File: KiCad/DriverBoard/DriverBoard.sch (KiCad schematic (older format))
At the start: 5 parts, among them J1 Conn_01x11, J2 Conn_01x05, J4 Conn_01x12, U1 Pico

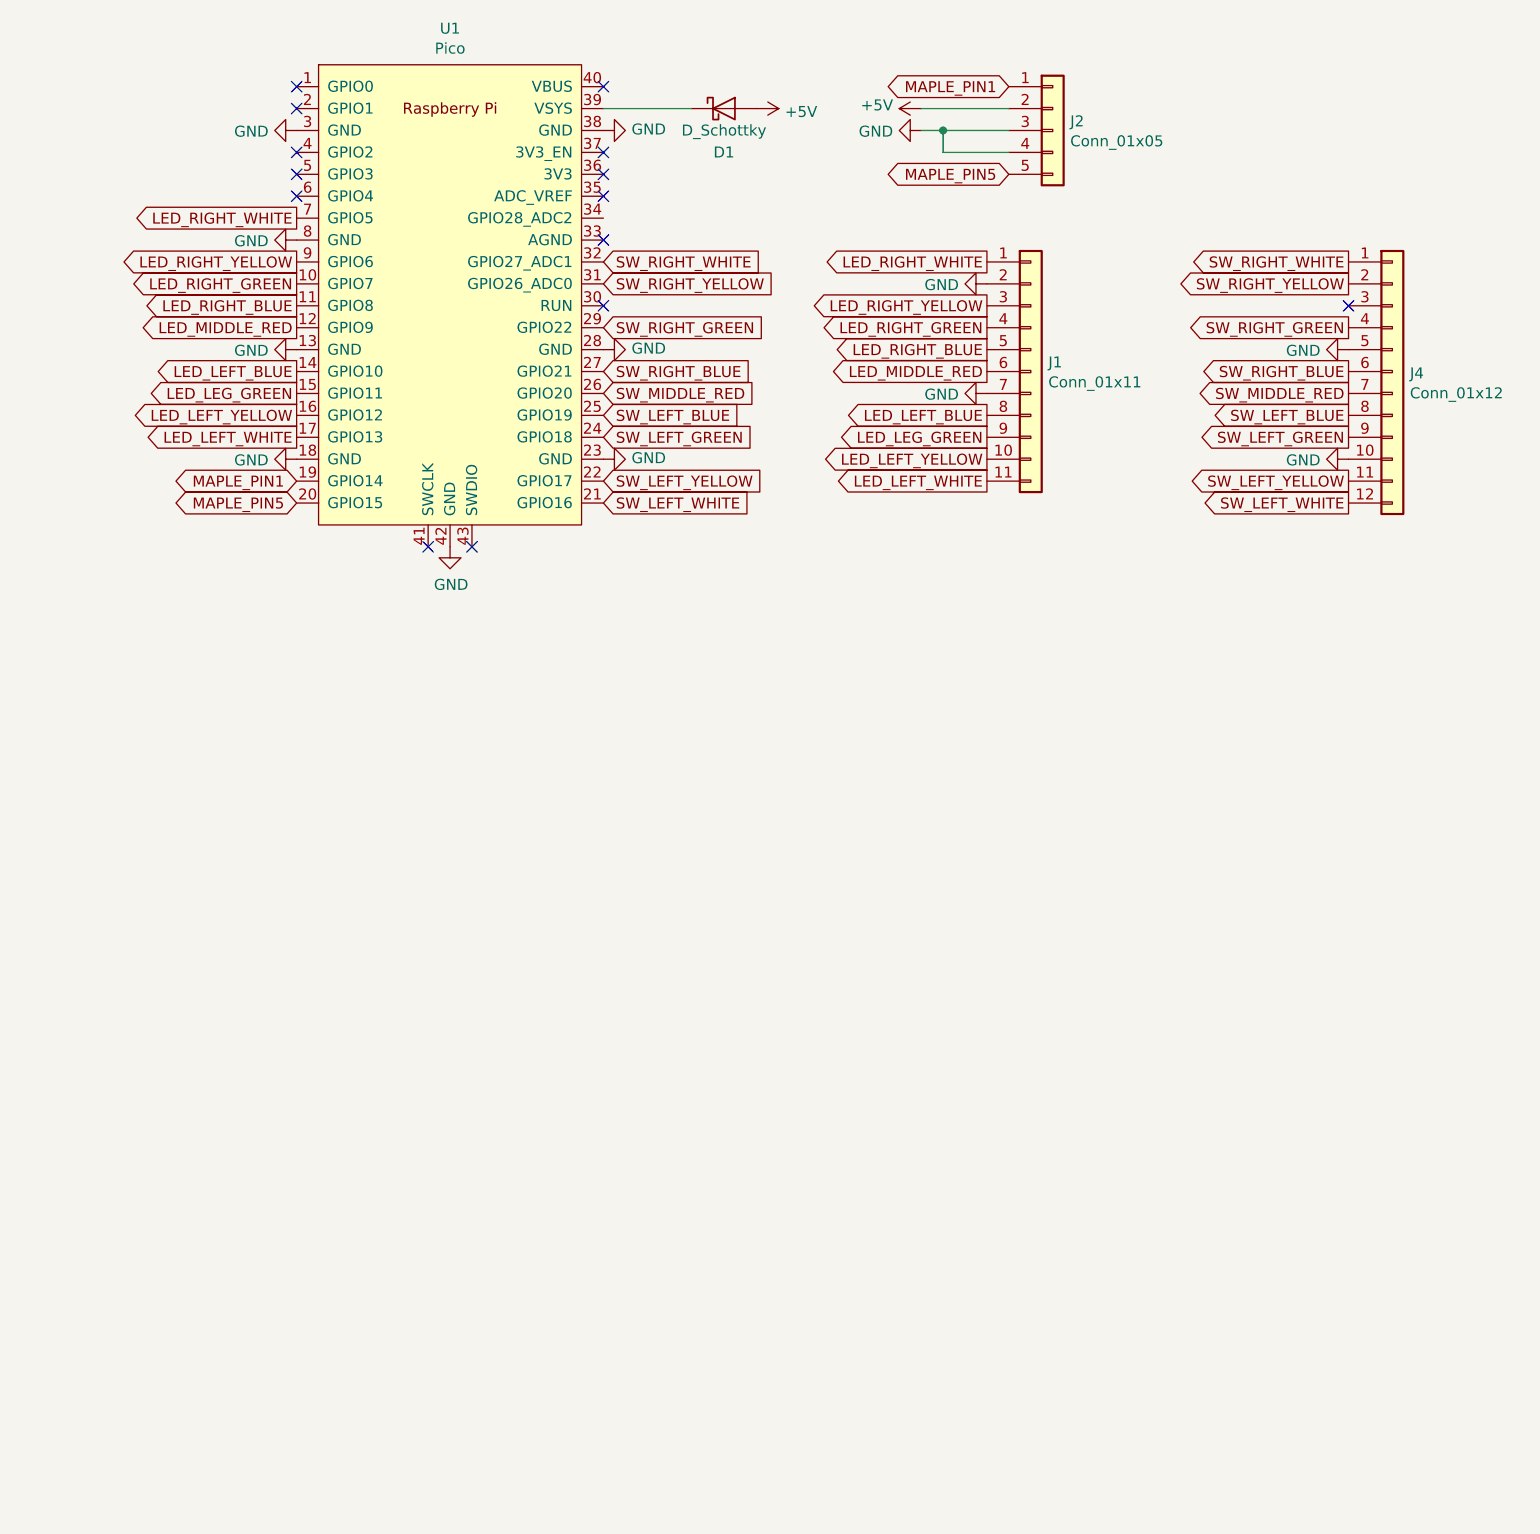
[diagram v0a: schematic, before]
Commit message: Added 5V LED drivers
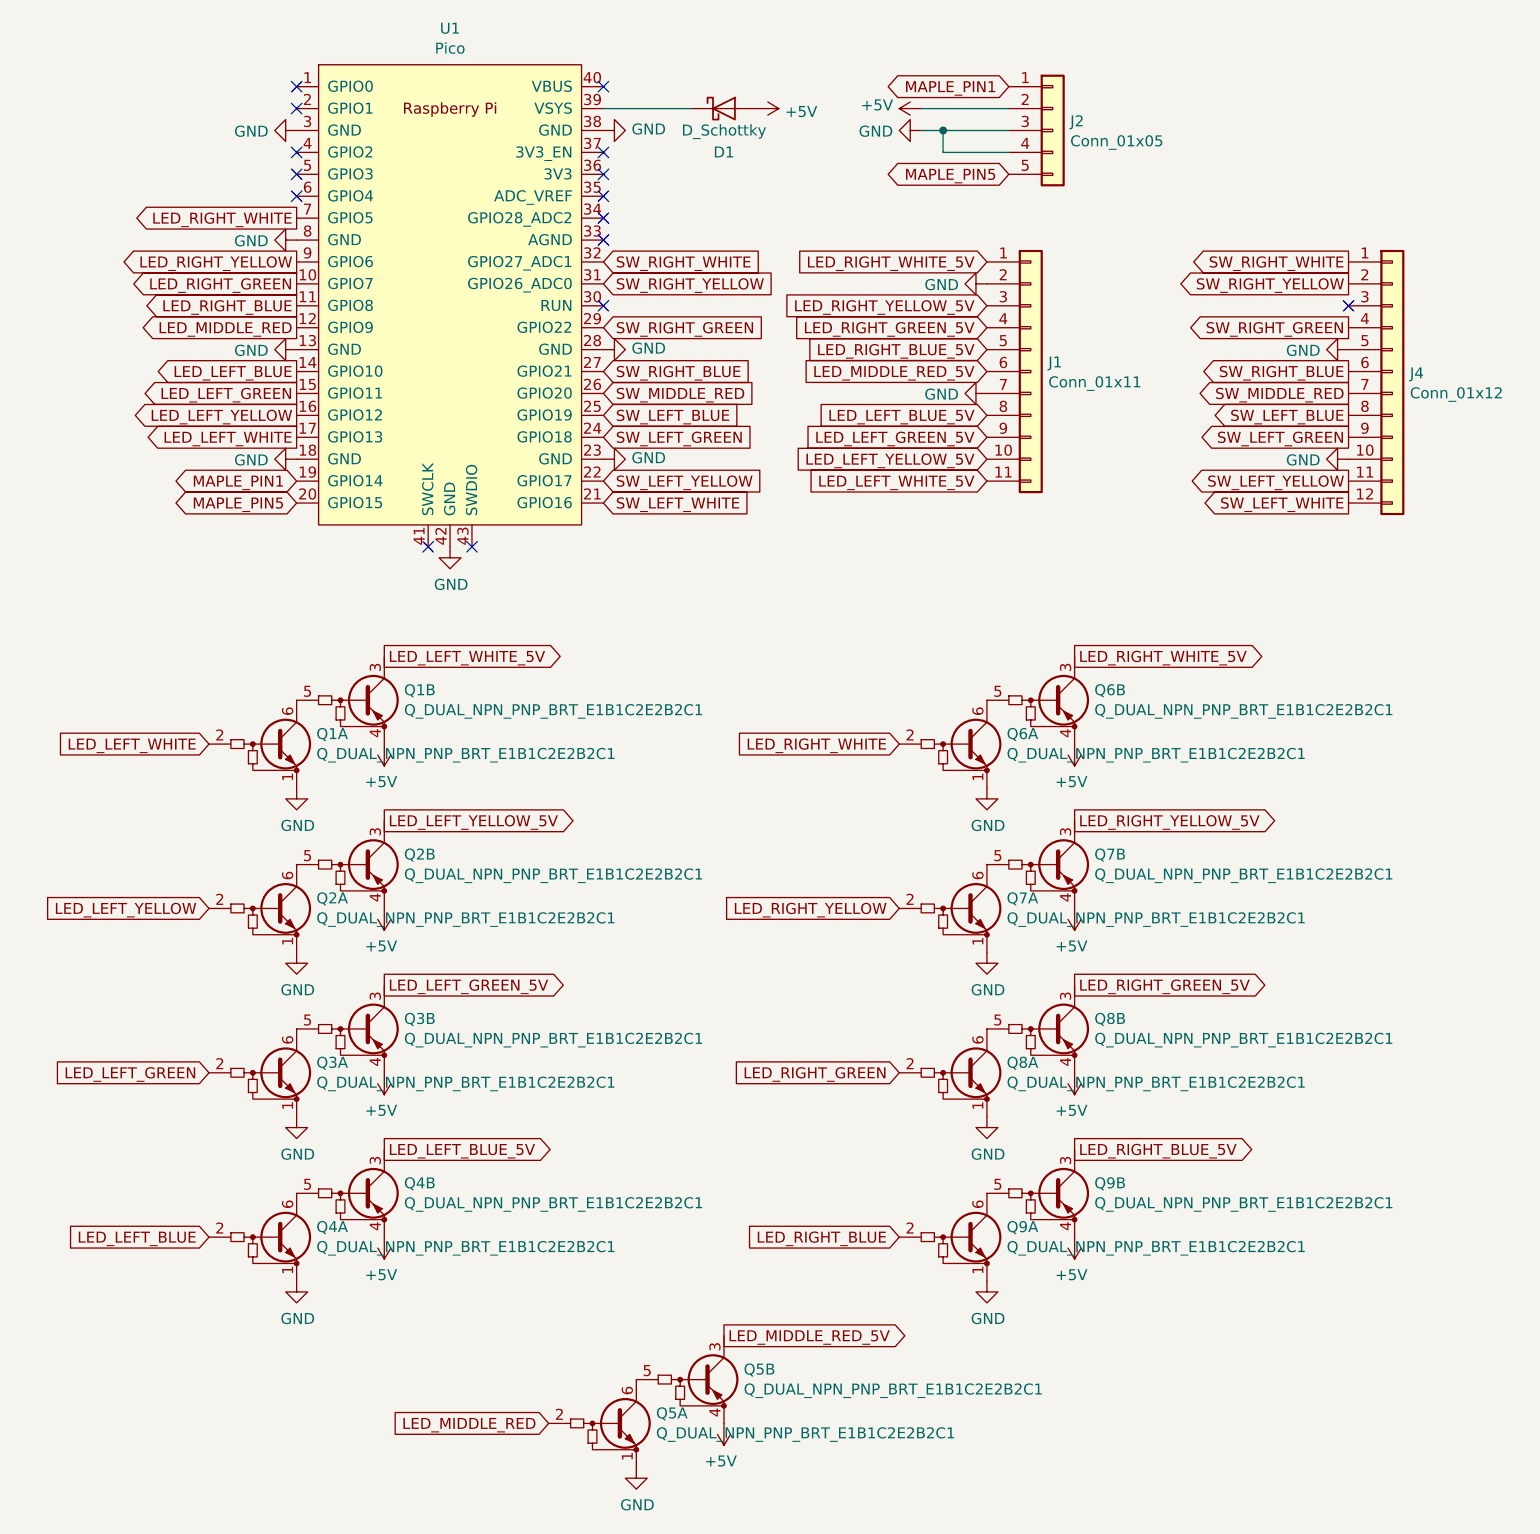
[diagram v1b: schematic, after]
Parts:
- added Q1, Q2, Q3, Q4, Q5, Q6, Q7, Q8, Q9: Q_DUAL_NPN_PNP_BRT_E1B1C2E2B2C1, Package_TO_SOT_SMD:SOT-363_SC-70-6_Handsoldering, symbol Device:Q_DUAL_NPN_PNP_BRT_E1B1C2E2B2C1
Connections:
- net +5V: now also Q1.4 (E1), Q2.4 (E1), Q3.4 (E1), Q4.4 (E1), Q5.4 (E1), Q6.4 (E1), Q7.4 (E1), Q8.4 (E1), Q9.4 (E1)
- net GND: now also Q1.1 (E1), Q2.1 (E1), Q3.1 (E1), Q4.1 (E1), Q5.1 (E1), Q6.1 (E1), Q7.1 (E1), Q8.1 (E1), Q9.1 (E1)
- net LED_LEFT_BLUE: now also Q4.2 (B1); no longer J1.8 (Pin_8)
- net LED_LEFT_WHITE: now also Q1.2 (B1); no longer J1.11 (Pin_11)
- net LED_LEFT_YELLOW: now also Q2.2 (B1); no longer J1.10 (Pin_10)
- net LED_MIDDLE_RED: now also Q5.2 (B1); no longer J1.6 (Pin_6)
- net LED_RIGHT_BLUE: now also Q9.2 (B1); no longer J1.5 (Pin_5)
- net LED_RIGHT_GREEN: now also Q8.2 (B1); no longer J1.4 (Pin_4)
- net LED_RIGHT_WHITE: now also Q6.2 (B1); no longer J1.1 (Pin_1)
- net LED_RIGHT_YELLOW: now also Q7.2 (B1); no longer J1.3 (Pin_3)
- net LED_LEG_GREEN renamed LED_LEFT_GREEN
- net LED_LEFT_GREEN: now also Q3.2 (B1); no longer J1.9 (Pin_9)
- new net: Q1.5 (B1), Q1.6 (C1)
- new net: Q3.5 (B1), Q3.6 (C1)
- new net: Q2.5 (B1), Q2.6 (C1)
- new net: Q4.5 (B1), Q4.6 (C1)
- new net: Q6.5 (B1), Q6.6 (C1)
- new net: Q8.5 (B1), Q8.6 (C1)
- new net: Q7.5 (B1), Q7.6 (C1)
- new net: Q9.5 (B1), Q9.6 (C1)
- new net: Q5.5 (B1), Q5.6 (C1)
- new net LED_LEFT_BLUE_5V: J1.8 (Pin_8), Q4.3 (C1)
- new net LED_LEFT_GREEN_5V: J1.9 (Pin_9), Q3.3 (C1)
- new net LED_LEFT_WHITE_5V: J1.11 (Pin_11), Q1.3 (C1)
- new net LED_LEFT_YELLOW_5V: J1.10 (Pin_10), Q2.3 (C1)
- new net LED_MIDDLE_RED_5V: J1.6 (Pin_6), Q5.3 (C1)
- new net LED_RIGHT_BLUE_5V: J1.5 (Pin_5), Q9.3 (C1)
- new net LED_RIGHT_GREEN_5V: J1.4 (Pin_4), Q8.3 (C1)
- new net LED_RIGHT_WHITE_5V: J1.1 (Pin_1), Q6.3 (C1)
- new net LED_RIGHT_YELLOW_5V: J1.3 (Pin_3), Q7.3 (C1)
- no-connect marks 14 -> 15
